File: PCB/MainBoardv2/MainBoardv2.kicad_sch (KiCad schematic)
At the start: 66 parts, among them J1 Conn_02x03_Odd_Even, J10 Conn_01x04_Socket, J2 USB_B_Micro, J3 Conn_02x03_Odd_Even, J4 Conn_01x05_Pin, J5 Conn_01x03_Socket, J6 Screw_Terminal_01x02, J7 Conn_01x04_Socket, J8 Screw_Terminal_01x02, J9 Conn_01x04_Socket, SW1 SW_Push, U1 AZ1117-3.3, U2 STM32F103C8T6TR, U3 SN74HCS4075PWR, U4 TPS56637RPA, Y1 8MHz Crystal

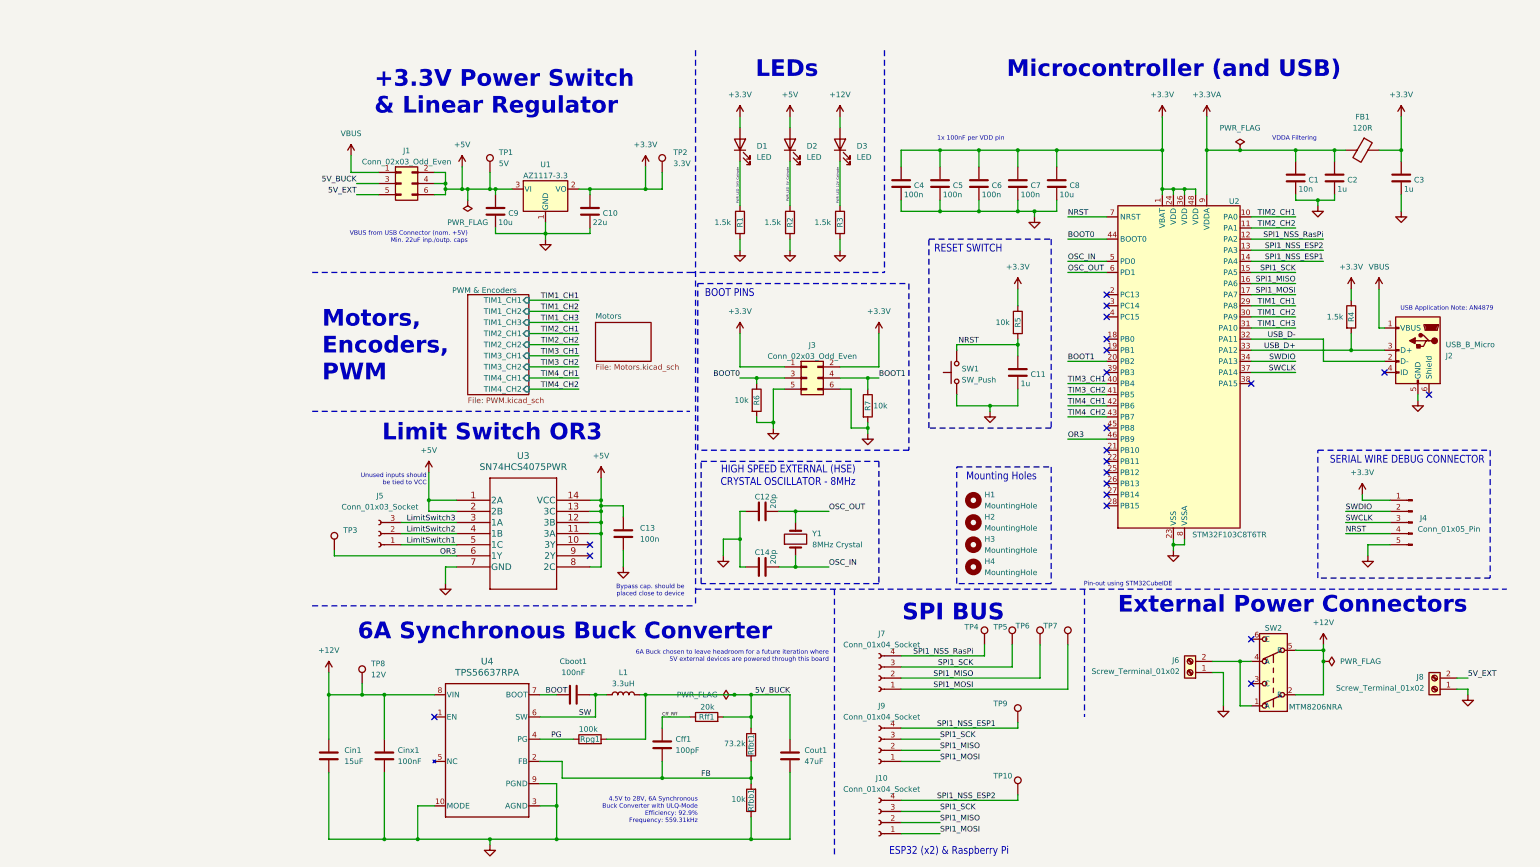
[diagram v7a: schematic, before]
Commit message: Updated part assignments on board for digikey order
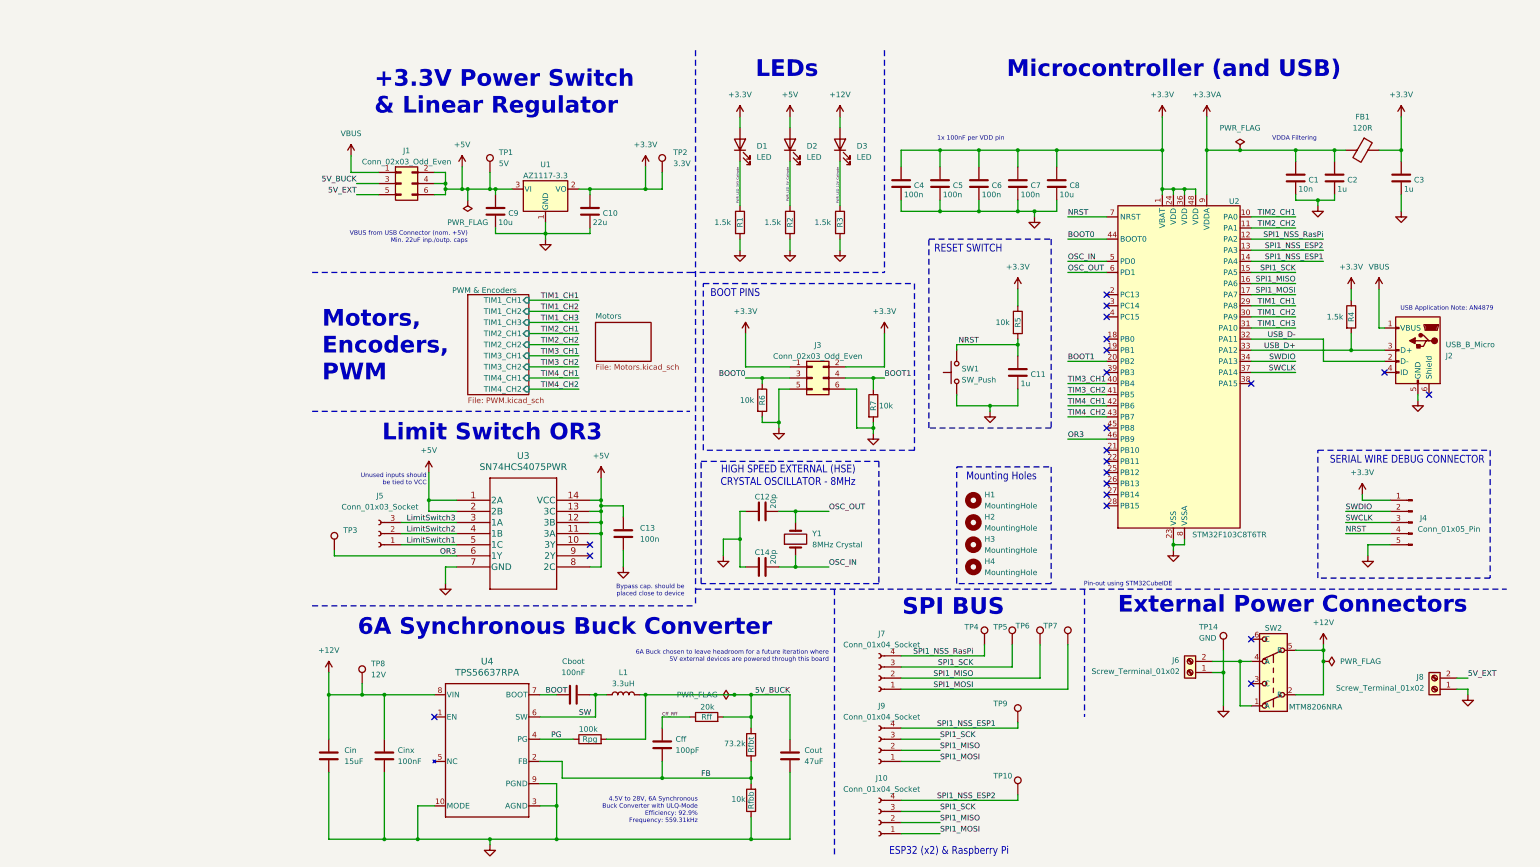
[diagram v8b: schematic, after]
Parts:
- added TP14: GND, TestPoint:TestPoint_Keystone_5000-5004_Miniature, symbol Connector:TestPoint
- SW2: value ~ -> Toggle
- TP10, TP4, TP5, TP6, TP7, TP9: value ~ -> Orange
- TP3: value ~ -> White
- renumbered Cboot1 to Cboot, Cff1 to Cff, Cin1 to Cin, Cinx1 to Cinx, Cout1 to Cout, Rfbb1 to Rfbb, Rfbt1 to Rfbt, Rff1 to Rff, Rpg1 to Rpg
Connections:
- net GND: now also TP14.1
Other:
- moved on the sheet: J3, R6, R7
